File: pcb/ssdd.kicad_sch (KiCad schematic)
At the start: 6 parts, among them U1 ATtiny861-20S

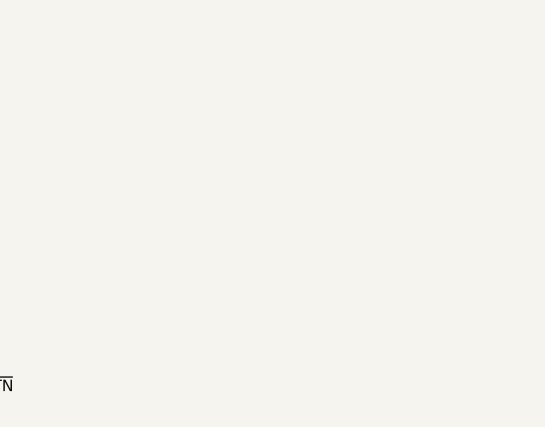
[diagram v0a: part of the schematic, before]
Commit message: module subsheet
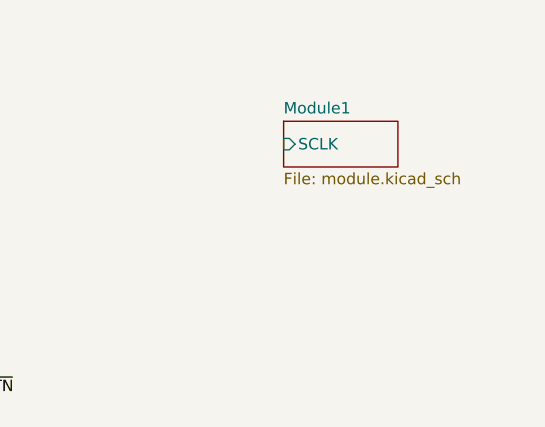
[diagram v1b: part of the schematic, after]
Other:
- added sheet Module1 (module.kicad_sch)
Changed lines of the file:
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@@
+		)
+	)
+	(sheet
+		(at 119.38 36.83)
+		(size 12.7 5.08)
+		(exclude_from_sim no)
+		(in_bom yes)
+		(on_board yes)
+		(dnp no)
+		(fields_autoplaced yes)
+		(stroke
+			(width 0.1524)
+			(type solid)
+		)
+		(fill
+			(color 0 0 0 0.0000)
+		)
+		(property "Sheetname" "Module1"
+			(at 119.38 36.1184 0)
+			(effects
+				(font
+					(size 1.27 1.27)
+				)
+				(justify left bottom)
+			)
+		)
+		(property "Sheetfile" "module.kicad_sch"
+			(at 119.38 42.4946 0)
+			(effects
+				(font
+					(size 1.27 1.27)
+				)
+				(justify left top)
+			)
+		)
+		(pin "SCLK" input
+			(at 119.38 39.37 180)
+			(effects
+				(font
+					(size 1.27 1.27)
+				)
+				(justify left)
+			)
+		)
+		(instances
+			(project "ssdd"
+				(path "/be5c4baa-09c6-44d9-9a7a-613f890eb055"
+					(page "2")
+				)
+			)
 		)
 	)

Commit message: tm1640 capacitors according to datasheet
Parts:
- added R2: 10K, symbol Device:R
- R1: value 1K -> 10K
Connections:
- net +5V: now also R2.2
- net 1640_DIN: now also R2.1
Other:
- moved on the sheet: DEC, ICSP, INC, R1, SET, U1

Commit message: connect modules
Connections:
- net M8CLK: now reaches U1.11 (PA7)
- net M7CLK: now reaches U1.12 (PA6)
- net M6CLK: now reaches U1.13 (PA5)
- net M5CLK: now reaches U1.14 (PA4)
- net M4CLK: now reaches U1.17 (AREF/PA3)
- net M3CLK: now reaches U1.18 (PA2)
- net M2CLK: now reaches U1.19 (PA1)
- net M1CLK: now reaches U1.20 (PA0)
- net M9CLK: now reaches U1.4 (PB3)
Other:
- added sheet Module2 (module.kicad_sch)
- added sheet Module3 (module.kicad_sch)
- added sheet Module4 (module.kicad_sch)
- added sheet Module5 (module.kicad_sch)
- added sheet Module6 (module.kicad_sch)
- added sheet Module7 (module.kicad_sch)
- added sheet Module8 (module.kicad_sch)
- added sheet Module9 (module.kicad_sch)
